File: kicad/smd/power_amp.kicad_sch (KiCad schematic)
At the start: 19 parts

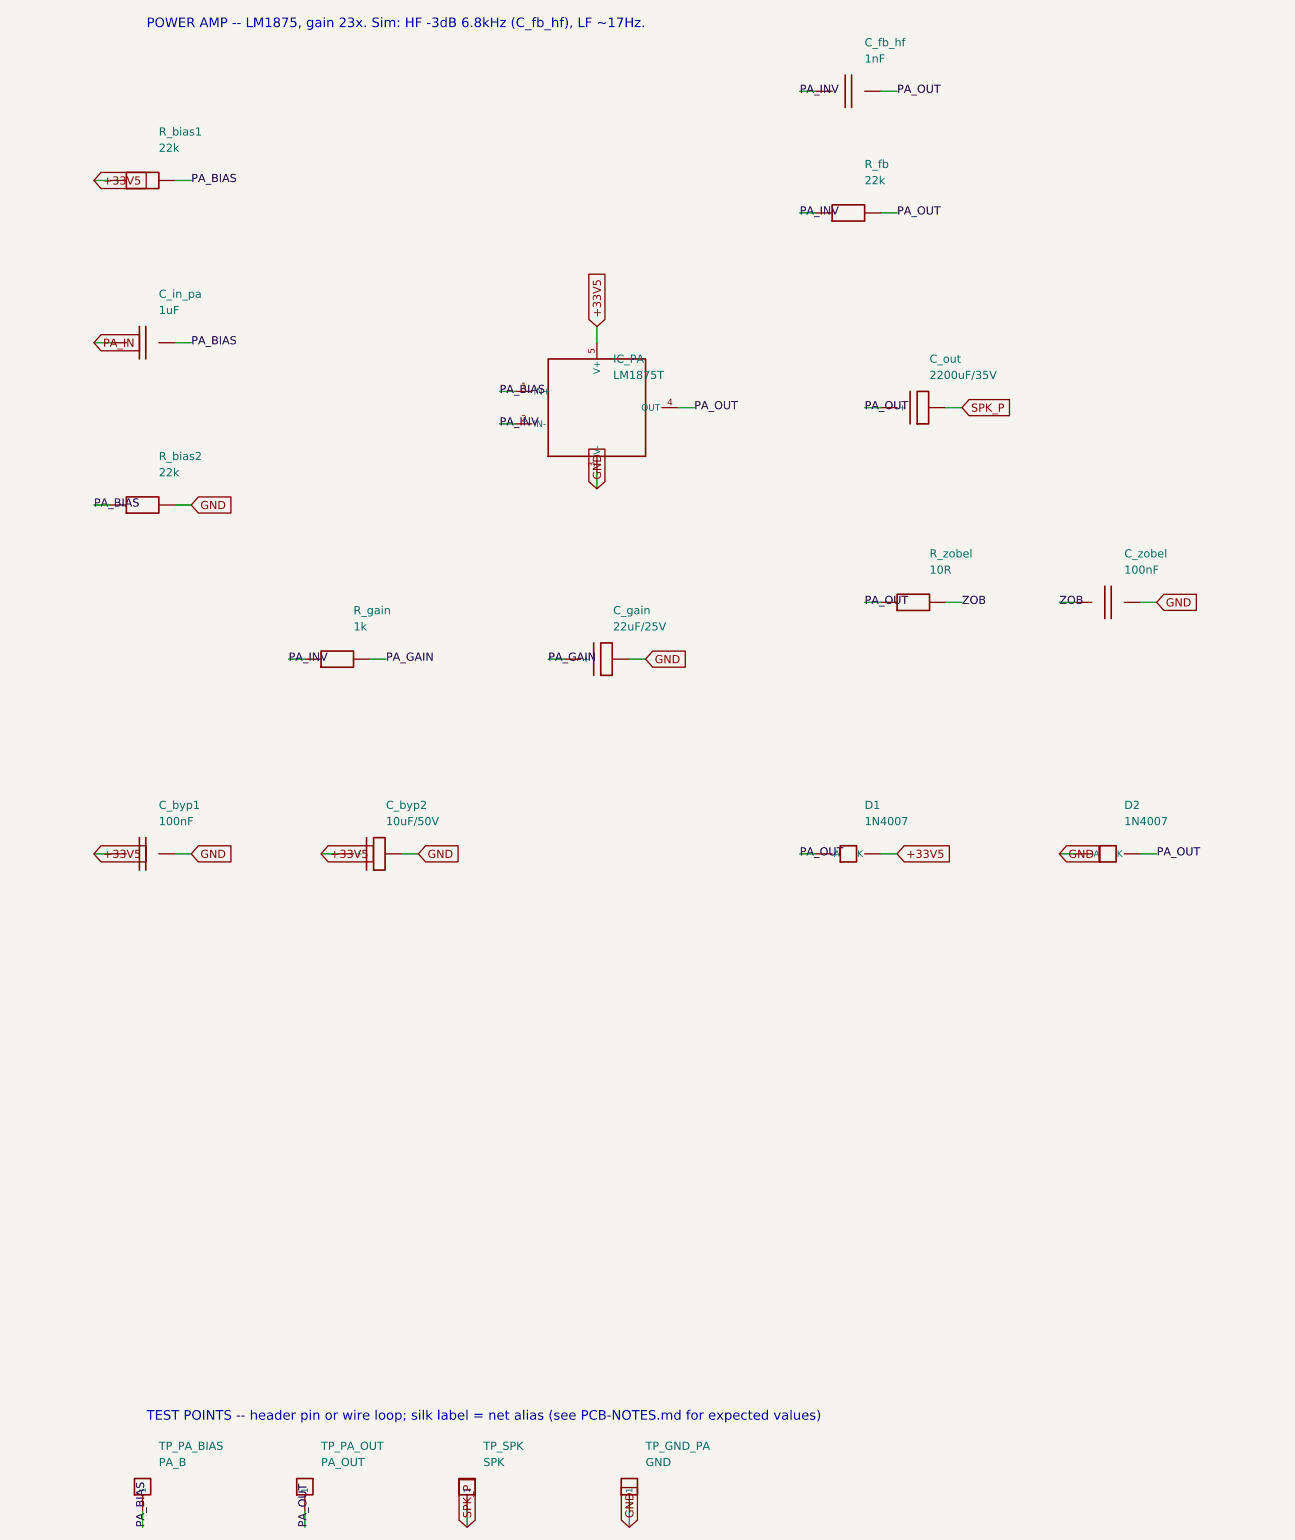
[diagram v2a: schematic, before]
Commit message: Noise, hum, crosstalk and thermal models; three design fixes; JLCPCB rules and cost
New models (docs/06c, spice/): a .noise run of the whole front end including the
LM317's own rail noise, the rail-ripple paths to the speaker, a vactrol-level tremolo
depth model, an electro-thermal LM1875 ladder, and a geometric crosstalk audit of the
routed boards (kicad/gen/crosstalk_audit.py). They found three defects:

- Errata #21 (hum + hiss): the LM1875 bias divider had no bypass (+4 dB ripple to
  speaker, 0.4 Vrms of 100 Hz at idle) and the LM317's 0.5 mV of noise reached the
  0 dB-PSRR JFET stages (23 dB above their floor, SNR 34 dB). Fixed with C_bref +
  R_bias3 on the power amp, C_adj on the regulator, and an RC-decoupled +17V_PRE rail
  for Q1/Q2/Q_rec: hum 408 mV -> 0.3 mV, EIN 37 -> 2.7 uV, SNR 34 -> 57 dB.
- Errata #22 (tremolo depth 1.7 dB): the vactrol LED was returned to ground from a
  mid-rail LFO -> 7 mA DC, a fixed -20 dB pad. LED limiter (2 V swing, LED_rate is one
  limiter LED) + Q_trem 2N3904/MMBT3904 emitter follower AC-coupled from the depth
  pot -> 15 dB depth, 0.8 dB insertion loss.
- Errata #23 (fab): stock TO-92 and the LM1875 footprint were under JLCPCB's 0.18 mm
  annular-ring minimum -> TO-92_Inline_Wide and 1.5 mm LM1875 pads; both .kicad_pro
  carry JLC's 2-layer limits as DRC constraints. Cost: all SMD caps 1206 (basic
  library), "(opt)" MRB caps DNP, gyrator on E24 values (same 1.86 H): 7 -> 2
  extended part types, ~$32 -> ~$17 assembly for five boards (kicad/gen/jlc_cost.py);
  three fiducials on the SMD board.

Crosstalk -> two routing rules (.kicad_dru: HighCurrent 0.6/0.4 mm and TankDrive
1.2/0.8 mm from signal copper, THT/SMD) that route_board.py also hands the router as
class clearances; keepout rule areas along the edge and around the mounting holes.
Thermal: Part 5's <= 2.5 K/W heatsink confirmed with numbers (Tj 97 C at 40 C ambient,
worst-case sine; 8-10 K/W clip-ons reach shutdown).

Placer: short parts stack beside tall ones i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
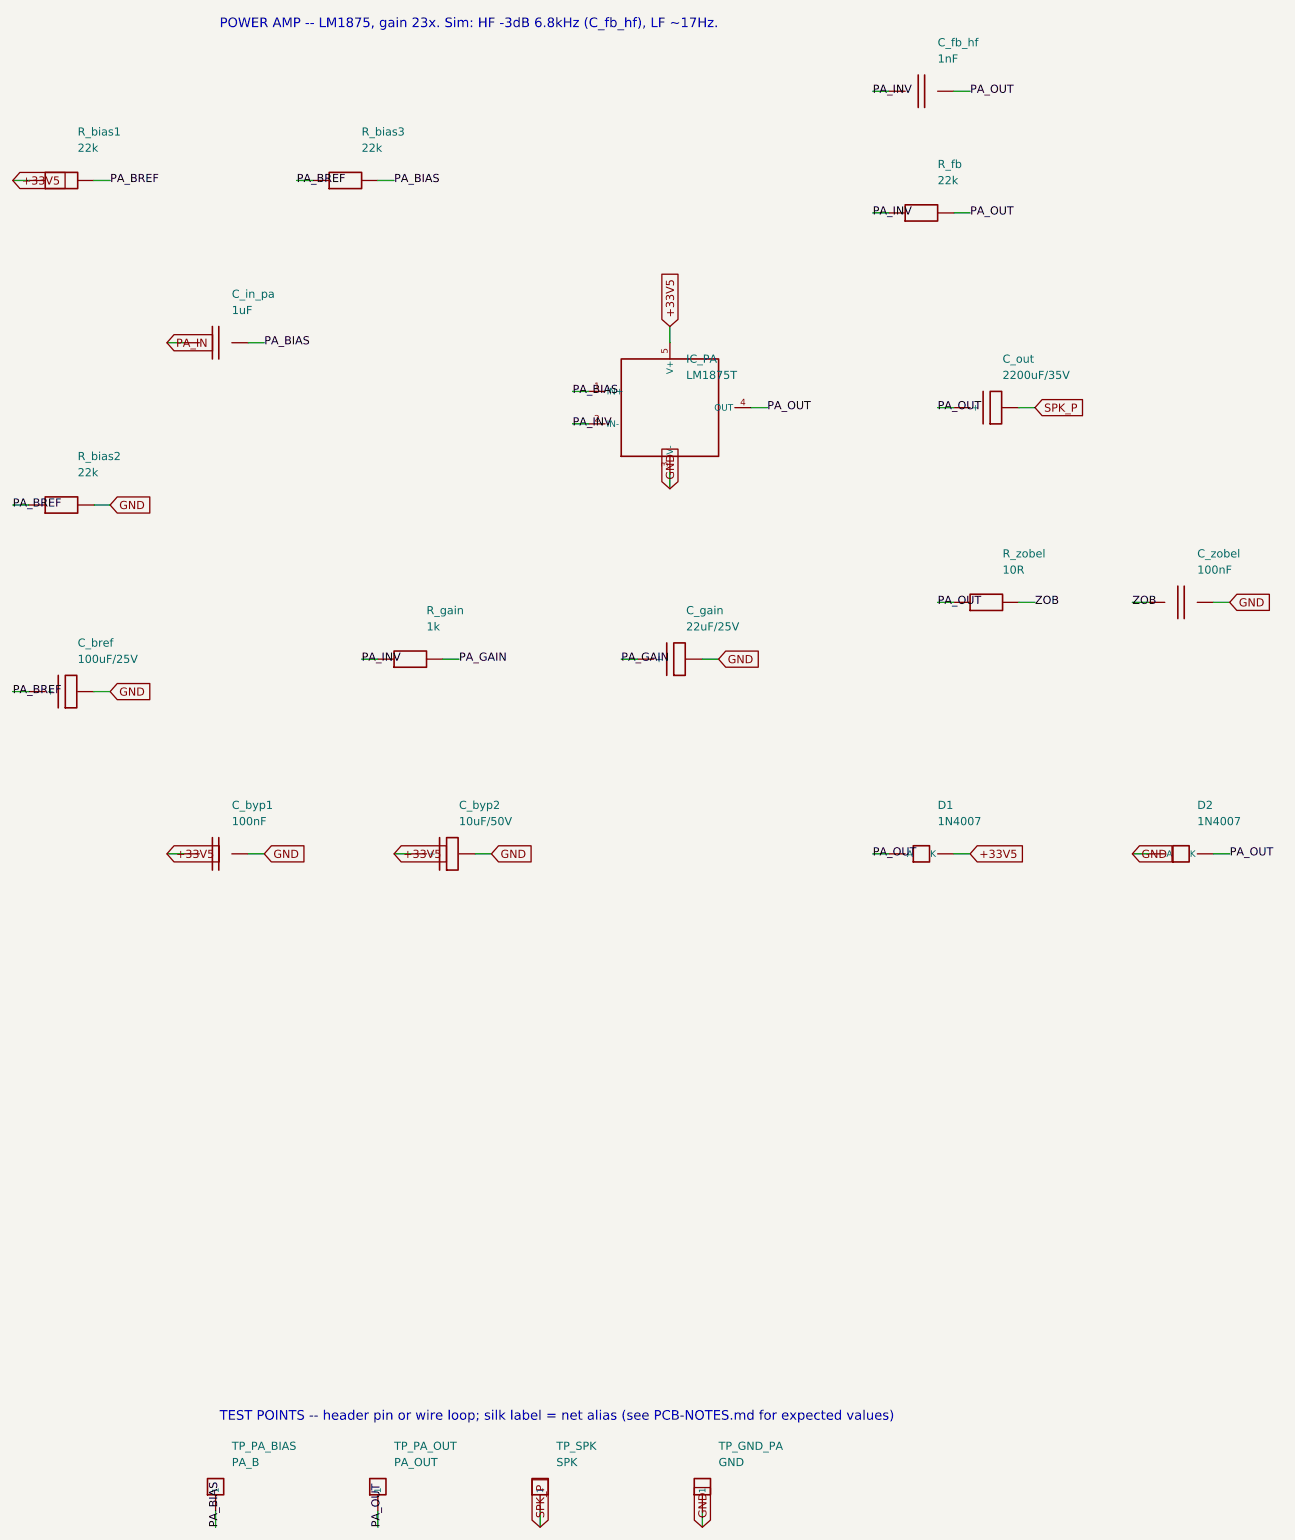
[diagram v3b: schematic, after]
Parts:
- added C_bref: 100uF/25V, Capacitor_THT:CP_Radial_D6.3mm_P2.50mm, symbol cr_primitives:CP
- added R_bias3: 22k, Resistor_SMD:R_0805_2012Metric, symbol cr_primitives:R
- C_in_pa, C_zobel: footprint Capacitor_SMD:C_1210_3225Metric -> Capacitor_SMD:C_1206_3216Metric
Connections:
- net GND: now also C_bref.2
- net PA_BIAS: now also R_bias3.2; no longer R_bias1.2, R_bias2.1
- new net PA_BREF: C_bref.1 (+), R_bias1.2, R_bias2.1, R_bias3.1
